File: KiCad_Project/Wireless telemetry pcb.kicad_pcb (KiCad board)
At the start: 2 copper layers, 38.9 x 93.2 mm, 21 parts, among them J1 Conn_02x10_Counter_Clockwise, J2 Conn_02x06_Counter_Clockwise, J3 Conn_01x02_Male, Q1 BSS138, Q2 BSS138, SW1 SW_Push, U1 LD1117V33, U2 ControllerBoardV1

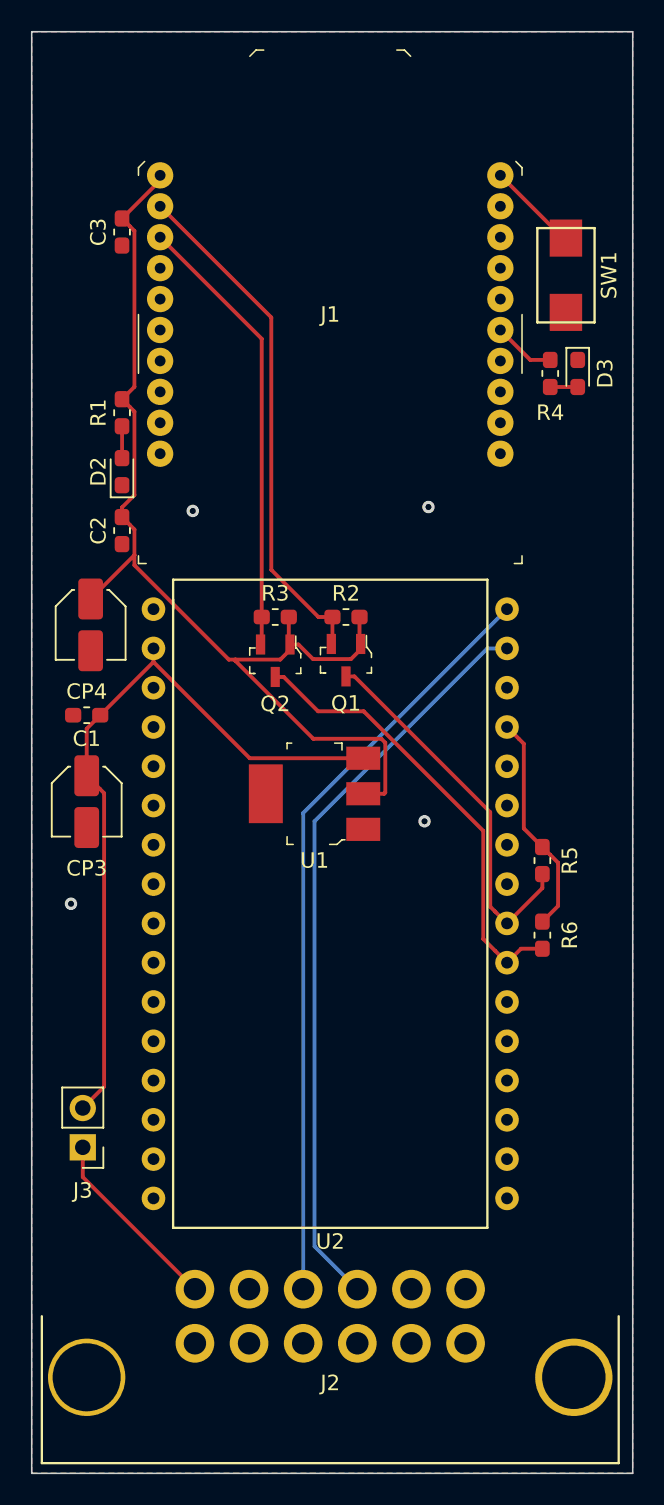
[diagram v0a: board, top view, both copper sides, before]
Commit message: Added mounting holes and silkscreen
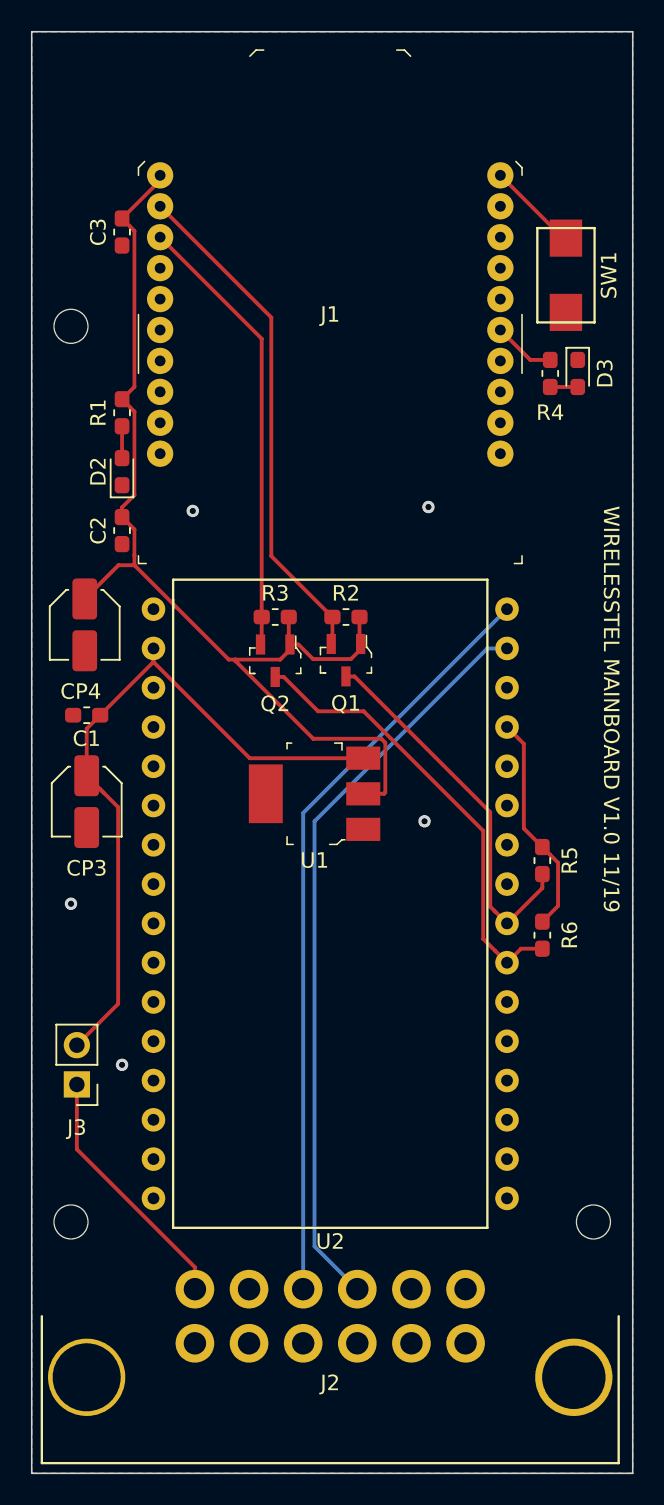
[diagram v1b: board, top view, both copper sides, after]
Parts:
- added REF**: MountingHole_2.2mm_M2, MountingHole:MountingHole_2.2mm_M2, F.Cu at (103.9, 41.4)
- added REF**: MountingHole_2.2mm_M2, MountingHole:MountingHole_2.2mm_M2, F.Cu at (103.9, 99.3)
- added REF**: MountingHole_2.2mm_M2, MountingHole:MountingHole_2.2mm_M2, F.Cu at (137.7, 99.3)
- moved J3 4.08 mm to (104.3, 90.4)
- moved CP4 0.38 mm to (104.8, 60.7)
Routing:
- net Net-(J2-Pad1): track 12.2 -> 16.4 mm
- net +12V: track 48.7 -> 45.9 mm
- net DOUT: track 33.5 -> 33.0 mm
- net GND: vias 4 -> 5
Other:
- board text added: "WIRELESSTEL MAINBOARD V1.0 11/19"
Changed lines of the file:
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@@
-(kicad_pcb (version 20171130) (host pcbnew "(5.1.4)-1")
+(kicad_pcb (version 20171130) (host pcbnew "(5.1.4-0-10_14)")
   (general
     (thickness 1.6)
-    (drawings 4)
-    (tracks 99)
+    (drawings 5)
+    (tracks 103)
     (zones 0)
-    (modules 21)
+    (modules 24)
     (nets 62)
   )
@@
     (mod_text_size 1 1)
     (mod_text_width 0.15)
-    (pad_size 3.8 2.2)
-    (pad_drill 0)
+    (pad_size 2.2 2.2)
+    (pad_drill 2.2)
     (pad_to_mask_clearance 0.051)
     (solder_mask_min_width 0.25)
@@
     (add_net Vcc5V)
   )
+  (module MountingHole:MountingHole_2.2mm_M2 (layer F.Cu)
+    (at 103.886 41.402)
+    (descr "Mounting Hole 2.2mm, no annular, M2")
+    (tags "mounting hole 2.2mm no annular m2")
+    (attr virtual)
+    (fp_text reference REF** (at 0 -3.2) (layer F.SilkS) hide
+      (effects (font (size 1 1) (thickness 0.15)))
+    )
+    (fp_text value MountingHole_2.2mm_M2 (at 0 3.2) (layer F.Fab)
+      (effects (font (size 1 1) (thickness 0.15)))
+    )
+    (fp_circle (center 0 0) (end 2.45 0) (layer F.CrtYd) (width 0.05))
+    (fp_circle (center 0 0) (end 2.2 0) (layer Cmts.User) (width 0.15))
+    (fp_text user %R (at 0.3 0) (layer F.Fab)
+      (effects (font (size 1 1) (thickness 0.15)))
+    )
+    (pad "" np_thru_hole circle (at 0 0) (size 2.2 2.2) (drill 2.2) (layers *.Cu *.Mask))
+  )
+  (module MountingHole:MountingHole_2.2mm_M2 (layer F.Cu)
+    (at 103.886 99.314)
+    (descr "Mounting Hole 2.2mm, no annular, M2")
+    (tags "mounting hole 2.2mm no annular m2")
+    (attr virtual)
+    (fp_text reference REF** (at 0 -3.2) (layer F.SilkS) hide
+      (effects (font (size 1 1) (thickness 0.15)))
+    )
+    (fp_text value MountingHole_2.2mm_M2 (at 0 3.2) (layer F.Fab)
+      (effects (font (size 1 1) (thickness 0.15)))
+    )
+    (fp_text user %R (at 0.3 0) (layer F.Fab)
+      (effects (font (size 1 1) (thickness 0.15)))
+    )
+    (fp_circle (center 0 0) (end 2.2 0) (layer Cmts.User) (width 0.15))
+    (fp_circle (center 0 0) (end 2.45 0) (layer F.CrtYd) (width 0.05))
+    (pad "" np_thru_hole circle (at 0 0) (size 2.2 2.2) (drill 2.2) (layers *.Cu *.Mask))
+  )
+  (module MountingHole:MountingHole_2.2mm_M2 (layer F.Cu)
+    (at 137.668 99.314)
+    (descr "Mounting Hole 2.2mm, no annular, M2")
+    (tags "mounting hole 2.2mm no annular m2")
+    (attr virtual)
+    (fp_text reference REF** (at 0 -3.2) (layer F.SilkS) hide
+      (effects (font (size 1 1) (thickness 0.15)))
+    )
+    (fp_text value MountingHole_2.2mm_M2 (at 0 3.2) (layer F.Fab)
+      (effects (font (size 1 1) (thickness 0.15)))
+    )
+    (fp_circle (center 0 0) (end 2.45 0) (layer F.CrtYd) (width 0.05))
+    (fp_circle (center 0 0) (end 2.2 0) (layer Cmts.User) (width 0.15))
+    (fp_text user %R (at 0.3 0) (layer F.Fab)
+      (effects (font (size 1 1) (thickness 0.15)))
+    )
+    (pad 1 np_thru_hole circle (at 0 0) (size 2.2 2.2) (drill 2.2) (layers *.Cu *.Mask))
+  )
   (module Lukas_Library:Breadboard_Center_32pin (layer F.Cu)
     (at 109.22 59.69)
@@
   )
   (module Connector_PinHeader_2.54mm:PinHeader_1x02_P2.54mm_Vertical (layer F.Cu)
-    (at 104.648 94.488 180)
+    (at 104.267 90.424 180)
     (descr "Through hole straight pin header, 1x02, 2.54mm pitch, single row")
     (tags "Through hole pin header THT 1x02 2.54mm single row")
@@
   )
   (module Capacitor_SMD:C_Elec_4x5.4 (layer F.Cu)
-    (at 105.156 60.706 270)
+    (at 104.775 60.706 270)
     (descr "SMD capacitor, aluminum electrolytic nonpolar, 4.0x5.4mm")
     (tags "capacitor electrolyic nonpolar")
@@
       (net 10 AD0\DIO0\CommissioningPushbutton))
   )
+  (gr_text "WIRELESSTEL MAINBOARD V1.0 11/19" (at 138.811 66.167 270) (layer F.SilkS)
+    (effects (font (size 1 1) (thickness 0.15)))
+  )
   (gr_line (start 140.208 22.352) (end 140.208 115.57) (layer Edge.Cuts) (width 0.1))
   (gr_line (start 101.346 22.352) (end 140.208 22.352) (layer Edge.Cuts) (width 0.1))
@@
   (segment (start 107.98801 54.53501) (end 107.687072 54.234072) (width 0.25) (layer F.Cu) (net 1))
   (segment (start 107.98801 56.19899) (end 107.98801 54.53501) (width 0.25) (layer F.Cu) (net 1))
-  (segment (start 105.156 59.031) (end 107.98801 56.19899) (width 0.25) (layer F.Cu) (net 1))
   (segment (start 107.687072 46.614072) (end 107.188 46.115) (width 0.25) (layer F.Cu) (net 1))
   (segment (start 107.98801 46.91501) (end 107.687072 46.614072) (width 0.25) (layer F.Cu) (net 1))
@@
   (segment (start 114.089763 62.951001) (end 114.513001 62.951001) (width 0.25) (layer F.Cu) (net 1))
   (segment (start 114.513001 62.951001) (end 117.418999 62.951001) (width 0.25) (layer F.Cu) (net 1))
+  (segment (start 106.956752 56.849248) (end 104.775 59.031) (width 0.25) (layer F.Cu) (net 1))
+  (segment (start 107.98801 56.849248) (end 106.956752 56.849248) (width 0.25) (layer F.Cu) (net 1))
   (segment (start 104.902 67.423) (end 105.777 66.548) (width 0.25) (layer F.Cu) (net 2))
   (segment (start 104.902 70.461) (end 104.902 67.423) (width 0.25) (layer F.Cu) (net 2))
@@
   (segment (start 115.443 69.328) (end 122.784 69.328) (width 0.25) (layer F.Cu) (net 2))
   (segment (start 109.22 63.105) (end 115.443 69.328) (width 0.25) (layer F.Cu) (net 2))
+  (segment (start 106.02701 71.58601) (end 105.77271 71.33171) (width 0.25) (layer F.Cu) (net 2))
   (segment (start 105.77271 71.33171) (end 104.902 70.461) (width 0.25) (layer F.Cu) (net 2))
-  (segment (start 106.02701 71.58601) (end 105.77271 71.33171) (width 0.25) (layer F.Cu) (net 2))
-  (segment (start 104.648 91.948) (end 106.02701 90.56899) (width 0.25) (layer F.Cu) (net 2))
-  (segment (start 106.02701 90.56899) (end 106.02701 71.58601) (width 0.25) (layer F.Cu) (net 2))
+  (segment (start 106.934 72.493) (end 105.77271 71.33171) (width 0.25) (layer F.Cu) (net 2))
+  (segment (start 106.934 85.217) (end 106.934 72.493) (width 0.25) (layer F.Cu) (net 2))
+  (segment (start 104.267 87.884) (end 106.934 85.217) (width 0.25) (layer F.Cu) (net 2))
   (segment (start 107.188 49.925) (end 107.188 47.865) (width 0.25) (layer F.Cu) (net 3))
   (segment (start 134.874 45.325) (end 136.652 45.325) (width 0.25) (layer F.Cu) (net 4))
   (segment (start 120.791 61.867) (end 120.716 61.942) (width 0.25) (layer F.Cu) (net 5))
   (segment (start 120.791 60.198) (end 120.791 61.867) (width 0.25) (layer F.Cu) (net 5))
-  (segment (start 119.888 60.198) (end 120.791 60.198) (width 0.25) (layer F.Cu) (net 5))
-  (segment (start 116.84 57.15) (end 119.888 60.198) (width 0.25) (layer F.Cu) (net 5))
+  (segment (start 120.777 60.198) (end 120.791 60.198) (width 0.25) (layer F.Cu) (net 5))
+  (segment (start 116.84 56.261) (end 120.777 60.198) (width 0.25) (layer F.Cu) (net 5))
+  (segment (start 116.84 40.83) (end 116.84 56.261) (width 0.25) (layer F.Cu) (net 5))
   (segment (start 109.65 33.64) (end 116.84 40.83) (width 0.25) (layer F.Cu) (net 5))
-  (segment (start 116.84 40.83) (end 116.84 57.15) (width 0.25) (layer F.Cu) (net 5))
   (segment (start 134.366 77.724) (end 134.366 76.821) (width 0.25) (layer F.Cu) (net 6))
   (segment (start 132.08 80.01) (end 134.366 77.724) (width 0.25) (layer F.Cu) (net 6))
@@
   (via (at 111.76 53.34) (size 0.8) (drill 0.4) (layers F.Cu B.Cu) (net 59))
   (via (at 103.886 78.74) (size 0.8) (drill 0.4) (layers F.Cu B.Cu) (net 59))
-  (segment (start 104.648 96.408) (end 104.648 94.488) (width 0.25) (layer F.Cu) (net 60))
-  (segment (start 111.9 103.66) (end 104.648 96.408) (width 0.25) (layer F.Cu) (net 60))
+  (via (at 107.188 89.154) (size 0.8) (drill 0.4) (layers F.Cu B.Cu) (net 59))
+  (segment (start 111.9 102.248) (end 111.9 103.66) (width 0.25) (layer F.Cu) (net 60))
+  (segment (start 104.267 94.615) (end 111.9 102.248) (width 0.25) (layer F.Cu) (net 60))
+  (segment (start 104.267 90.424) (end 104.267 94.615) (width 0.25) (layer F.Cu) (net 60))
   (segment (start 134.865072 75.570072) (end 134.366 75.071) (width 0.25) (layer F.Cu) (net 61))
   (segment (start 135.382 76.087) (end 134.865072 75.570072) (width 0.25) (layer F.Cu) (net 61))
